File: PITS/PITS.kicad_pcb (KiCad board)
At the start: 4 copper layers, 65 x 56 mm, 75 parts, among them P1 CONN_02X20, P10 I2C, P11 I2C, P12 I2C, P13 I2C, P14 BATT, P2 BNC, P3 BNC, P4 BNC, P5 BNC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

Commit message: first finished layout
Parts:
- removed P10, P11, P12, P13: I2C, Socket_Strips:Socket_Strip_Straight_1x04
- removed P7, P8, P9: 1-WIRE, Socket_Strips:Socket_Strip_Straight_1x03
- removed Q3: BC557, TO_SOT_Packages_SMD:SOT-23
- removed R24, R25, R8: 4k7, Resistors_SMD:R_0805_HandSoldering
- added U8: BME280, RF_Modules:BME280, F.Cu at (95.9, 75.0)
- C1, C2, C4: footprint Capacitors_SMD:C_0805_HandSoldering -> Capacitors_SMD:C_0603_HandSoldering; moved to B.Cu
- C10, C11, C12, C13, C15, C16, C17, C3, C9, L2, Q1, R10, R11, R16, R17, R18, R7, R9, U5: moved to B.Cu
- C14: footprint Capacitors_SMD:C_0805_HandSoldering -> Capacitors_SMD:C_0603_HandSoldering
- D1, D2, D3, D4, D5, D6: footprint LEDs:LED_0805 -> LEDs:LED_0603
- P14: footprint Connectors_Terminal_Blocks:TerminalBlock_Pheonix_MKDS1.5-2pol -> Connectors:SMD_2
- Q2: value BC557 -> Q_PNP_dual; footprint TO_SOT_Packages_SMD:SOT-23 -> TO_SOT_Packages_SMD:SOT-23-6_Handsoldering; moved to B.Cu
- R1, R14, R15, R2, R20, R21, R22, R23, R26, R3, R4, R5: footprint Resistors_SMD:R_0805_HandSoldering -> Resistors_SMD:R_0603_HandSoldering
- R12, R13, R19, R6: footprint Resistors_SMD:R_0805_HandSoldering -> Resistors_SMD:R_0603_HandSoldering; moved to B.Cu
- moved R9 102.3 mm to (84.5, 71.6), turned to 90 degrees
- moved R11 98.7 mm to (94.0, 72.7)
- moved C17 98.0 mm to (87.6, 61.5), turned to 90 degrees
- moved C9 93.9 mm to (99.7, 65.1), turned to 270 degrees
- moved R17 92.5 mm to (96.3, 56.5), turned to 0 degrees
- moved C10 92.1 mm to (85.1, 63.4), turned to 90 degrees
- moved R16 90.7 mm to (96.3, 58.4)
- moved L2 90.0 mm to (104.8, 68.6), turned to 90 degrees
- moved C15 89.6 mm to (93.3, 75.9)
- moved U5 89.4 mm to (93.1, 66.4)
- moved R18 88.4 mm to (96.3, 60.3), turned to 0 degrees
- moved C16 88.4 mm to (93.3, 59.4), turned to 270 degrees
- moved Q1 87.0 mm to (81.9, 61.4), turned to 180 degrees
- moved C3 86.7 mm to (99.7, 68.9), turned to 270 degrees
- moved C13 84.1 mm to (87.6, 68.9), turned to 90 degrees
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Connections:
- C13 pad 1: Net-(C12-Pad2) -> Net-(C13-Pad1)
- C13 pad 2: Net-(C13-Pad2) -> Net-(C12-Pad1)
- Q2 pad 3: +5V_PSU -> Net-(Q2-Pad1)
- R10 pad 1: Net-(C13-Pad2) -> Net-(C12-Pad2)
- R10 pad 2: Net-(C12-Pad1) -> Net-(C13-Pad1)
- R15 pad 1: /GPIO19(MISO1) -> /GPIO20(MOSI1)
- R16 pad 1: Net-(C13-Pad2) -> Net-(C12-Pad1)
- R17 pad 2: Net-(C13-Pad2) -> Net-(C12-Pad1)
- R18 pad 2: Net-(C13-Pad2) -> Net-(C12-Pad1)
- U1 pad 4: /GPIO23 -> /GPIO25
- U2 pad 16: /GPIO27 -> /GPIO16(CE2)
- U2 pad 17: /GPIO22 -> /GPIO19(MISO1)
- U2 pad 4: /GPIO20(MOSI1) -> /GPIO12
- U4 pad 14: /GPIO16(CE2) -> /GPIO22
- U4 pad 7: /GPIO12 -> /GPIO27
- U5 pad 2: Net-(C12-Pad2) -> Net-(C13-Pad1)
- U5 pad 3: Net-(C13-Pad2) -> Net-(C12-Pad1)
- U6 pad 14: /GPIO25 -> /GPIO24
- U6 pad 7: /GPIO24 -> /GPIO23
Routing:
- net GND: track 205.8 -> 483.5 mm, vias 0 -> 3
- net +3V3: track 2.61 -> 91.6 mm, vias 0 -> 4
- net /GPIO27: track 0.00 -> 54.3 mm, vias 0 -> 1
- net +BATT: track 16.5 -> 68.5 mm, vias 0 -> 4
- net /GPIO2(SDA1): track 0.00 -> 50.8 mm, vias 0 -> 4
- net /GPIO16(CE2): track 83.9 -> 33.4 mm, vias 0 -> 1
- net /GPIO3(SCL1): track 0.00 -> 42.1 mm, vias 0 -> 4
- net +5V: track 0.00 -> 38.6 mm
- net /GPIO22: track 0.00 -> 37.5 mm, vias 0 -> 1
- net /GPIO23: track 9.16 -> 37.4 mm, vias 0 -> 1
- net /GPIO12: track 58.4 -> 31.2 mm, vias 0 -> 1
- net /GPIO25: track 36.0 -> 9.14 mm
- net Net-(C12-Pad1): track 1.98 -> 24.0 mm, vias 0 -> 2
- net /GPIO24: track 35.3 -> 17.5 mm, vias 0 -> 1
- net Iout: track 0.00 -> 17.7 mm, vias 0 -> 2
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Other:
- copper layers 4 -> 2

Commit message: old layout - commit for backup
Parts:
- D3: value INTERNET_Green -> Inet_Green
- moved D1 10.5 mm to (99.1, 78.7)
- moved D5 10.5 mm to (109.2, 78.7)
- moved R14 10.2 mm to (99.1, 75.2)
- moved R22 10.2 mm to (109.2, 75.2)
- moved R5 7.29 mm to (81.3, 83.0), turned to 90 degrees
- moved R3 5.72 mm to (81.3, 78.9), turned to 90 degrees
- moved D2 5.68 mm to (101.6, 78.7)
- moved R15 5.18 mm to (101.6, 75.2)
- moved D3 3.59 mm to (106.7, 78.7)
- moved D4 3.59 mm to (104.1, 78.7)
- moved R20 2.74 mm to (106.7, 75.2)
- moved R21 2.74 mm to (104.1, 75.2)
- moved D6 2.54 mm to (111.8, 78.7)
- moved R23 1.03 mm to (111.8, 75.2)
- moved C14 1.00 mm to (96.5, 76.5)
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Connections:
- R14 pad 1: /GPIO26 -> /GPIO5
- R15 pad 1: /GPIO20(MOSI1) -> /GPIO6
- R20 pad 1: /GPIO13 -> /GPIO20(MOSI1)
- R21 pad 1: /GPIO6 -> /GPIO13
- R22 pad 1: /GPIO5 -> /GPIO26
- U2 pad 16: /GPIO16(CE2) -> /GPIO19(MISO1)
- U2 pad 17: /GPIO19(MISO1) -> /GPIO16(CE2)
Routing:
- net GND: track 483.5 -> 305.5 mm, vias 3 -> 1
- net +BATT: track 68.5 -> 6.12 mm, vias 4 -> 0
- net +3V3: track 91.6 -> 109.5 mm, vias 4 -> 5
- net /GPIO2(SDA1): track 50.8 -> 65.3 mm, vias 4 -> 3
- net Net-(R1-Pad1): track 7.76 -> 0.00 mm
- net /GPIO18: track 8.45 -> 1.27 mm, vias 1 -> 0
- net /GPIO15(RXD0): track 64.5 -> 58.7 mm, vias 4 -> 3
- net /GPIO9(MISO0): track 58.9 -> 62.2 mm
- net /GPIO11(SCLK0): track 65.8 -> 68.4 mm
- net /GPIO3(SCL1): track 42.1 -> 44.7 mm, vias 4 -> 3
- net Net-(L1-Pad2): track 2.54 -> 0.00 mm
- net /GPIO7(CE1): track 64.8 -> 67.1 mm
- net /GPIO14(TXD0): track 57.1 -> 59.5 mm, vias 5 -> 3
- net /GPIO25: track 9.14 -> 6.92 mm
- net /GPIO17: track 46.1 -> 43.9 mm
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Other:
- net class Default: trace_width 0.3556 -> 0.254; via_dia 0.5 -> 0.6096; via_drill 0.3 -> 0.3048
- net class POWER: clearance 0.2032 -> 0.03556; trace_width 0.9144 -> 0.6096; via_dia 0.7 -> 1.2192; via_drill 0.5 -> 0.6096
- rule via_min_drill: 0.3 -> 0.3048
- rule via_min_size: 0.4 -> 0.6096

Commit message: working on layout
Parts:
- added P10, P11, P12, P13: I2C, Socket_Strips:Socket_Strip_Straight_1x04, F.Cu at (87.5, 115.1)
- added P7, P8, P9: 1-WIRE, Socket_Strips:Socket_Strip_Straight_1x03, F.Cu at (87.5, 115.1)
- added R24, R25, R8: 4k7, Resistors_SMD:R_0603_HandSoldering, F.Cu at (87.5, 115.1)
- P2, P3, P4, P5, P6: footprint Connectors:SMA_Edge -> Connectors:SMA_Edge_small
- moved C10 145.2 mm to (224.1, 21.4)
- moved C11 145.2 mm to (236.2, 29.1)
- moved C12 145.2 mm to (225.0, 26.9)
- moved C13 145.2 mm to (226.6, 26.9)
- moved C16 145.2 mm to (232.3, 17.4)
- moved C17 145.2 mm to (226.6, 19.5)
- moved C3 145.2 mm to (238.7, 26.9)
- moved C9 145.2 mm to (238.7, 23.1)
- moved L2 145.2 mm to (243.8, 26.6)
- moved Q1 145.2 mm to (220.9, 19.4)
- moved Q2 145.2 mm to (220.9, 24.8)
- moved R10 145.2 mm to (226.5, 30.4)
- moved R11 145.2 mm to (233.0, 30.7)
- moved R16 145.2 mm to (235.3, 16.4)
- moved R18 145.2 mm to (235.3, 18.3)
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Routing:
- net GND: track 305.5 -> 0.00 mm, vias 1 -> 0
- net +3V3: track 109.5 -> 0.00 mm, vias 5 -> 0
- net /GPIO11(SCLK0): track 68.4 -> 0.00 mm, vias 2 -> 0
- net /GPIO7(CE1): track 67.1 -> 0.00 mm, vias 1 -> 0
- net /GPIO2(SDA1): track 65.3 -> 0.00 mm, vias 3 -> 0
- net /GPIO9(MISO0): track 62.2 -> 0.00 mm, vias 2 -> 0
- net /GPIO14(TXD0): track 59.5 -> 0.00 mm, vias 3 -> 0
- net /GPIO10(MOSI0): track 59.3 -> 0.00 mm, vias 2 -> 0
- net /GPIO15(RXD0): track 58.7 -> 0.00 mm, vias 3 -> 0
- net /GPIO27: track 54.2 -> 0.00 mm, vias 1 -> 0
- net /GPIO3(SCL1): track 44.7 -> 0.00 mm, vias 3 -> 0
- net /GPIO17: track 43.9 -> 0.00 mm, vias 1 -> 0
- net /GPIO8(CE0): track 41.7 -> 0.00 mm, vias 1 -> 0
- net +5V: track 37.6 -> 0.00 mm
- net /GPIO22: track 37.3 -> 0.00 mm, vias 1 -> 0
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
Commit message: layout - work in progress
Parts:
- moved U1 146.5 mm to (62.1, 65.8), turned to 270 degrees
- moved U6 87.9 mm to (72.9, 89.1)
- moved P4 64.6 mm to (117.6, 93.1), turned to 180 degrees
- moved P3 62.8 mm to (57.4, 68.4), turned to 0 degrees
- moved U4 52.6 mm to (72.9, 68.1)
- moved P2 36.8 mm to (92.6, 102.0), turned to 90 degrees
- moved U3 36.7 mm to (113.4, 93.6), turned to 90 degrees
- moved P5 31.4 mm to (57.4, 60.1)
- moved P6 17.6 mm to (57.4, 81.1)
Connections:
- net Net-(D1-Pad2) renamed /D1
- net Net-(D2-Pad2) renamed /D2
- net Net-(D3-Pad2) renamed /D3
- net Net-(D4-Pad2) renamed /D4
- net Net-(D5-Pad2) renamed /D5
- net Net-(D6-Pad2) renamed /D6
- net Net-(R2-Pad1) renamed /MTX2-TXD
- net Net-(R26-Pad2) renamed /HX1-TXD
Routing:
- net GND: track 0.00 -> 57.9 mm
- net Net-(P6-Pad1): track 0.00 -> 8.59 mm
- net Net-(P5-Pad1): track 0.00 -> 8.59 mm
- net Net-(P3-Pad1): track 0.00 -> 4.78 mm
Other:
- net class Analog added: clearance 0.2032, trace_width 0.254, via_dia 0.6096, via_drill 0.3048
- net class Digital added: clearance 0.254, trace_width 0.3556, via_dia 0.6096, via_drill 0.3048
- net class HF added: clearance 0.2032, trace_width 1.524, via_dia 0.6096, via_drill 0.3048
- net class NC added: clearance 0.2032, trace_width 0.254, via_dia 0.6096, via_drill 0.3048
- net class POWER: trace_width 0.6096 -> 1.524

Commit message: layout - work in progress
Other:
- net class Digital: clearance 0.254 -> 0.2032; trace_width 0.3556 -> 0.254
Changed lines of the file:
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@@
   (general
     (links 214)
-    (no_connects 193)
-    (area 54.924999 48.924999 120.075001 105.075001)
+    (no_connects 184)
+    (area 49.841238 13.491 251.289 118.294001)
     (thickness 1.6)
     (drawings 14)
@@
   )
   (net_class Digital ""
-    (clearance 0.254)
-    (trace_width 0.3556)
+    (clearance 0.2032)
+    (trace_width 0.254)
     (via_dia 0.6096)
     (via_drill 0.3048)

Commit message: layout - work in progress
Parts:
- removed C10: 10µ, Capacitors_SMD:C_1206_HandSoldering
- removed C11: 1µ, Capacitors_SMD:C_0603_HandSoldering
- removed C12: 680p, Capacitors_SMD:C_0603_HandSoldering
- removed C13, C15: 22p, Capacitors_SMD:C_0603_HandSoldering
- removed C16: 47p, Capacitors_SMD:C_0603_HandSoldering
- removed C17: 47µ, Capacitors_SMD:C_1206_HandSoldering
- removed C3, C9: 100n, Capacitors_SMD:C_0603_HandSoldering
- removed L2: 4.7µH, Inductors:Inductor_Wurth_HCI-7040
- removed R10, R11, R18: 10k, Resistors_SMD:R_0603_HandSoldering
- removed R16: 845k, Resistors_SMD:R_0603_HandSoldering
- removed R17: 158k, Resistors_SMD:R_0603_HandSoldering
- removed R7, R9: 1M, Resistors_SMD:R_0603_HandSoldering
- U5: value LTC3112 -> TPS61030; footprint Housings_SSOP:ETSSOP-20-1EP_4.4x6.5mm_Pitch0.65mm -> power:TPS61030
- moved U5 134.8 mm to (104.0, 66.5), turned to 180 degrees
- moved Q1 128.8 mm to (100.1, 63.9), turned to 270 degrees
- moved Q2 121.9 mm to (105.5, 63.9), turned to 180 degrees
- moved R6 116.2 mm to (110.3, 63.2), turned to 0 degrees
- moved R19 115.0 mm to (110.3, 65.1), turned to 0 degrees
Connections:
- U5 pad 1: GND -> +BATT
- U5 pad 2: Net-(C13-Pad1) -> GND
- U5 pad 3: Net-(C12-Pad1) -> +5V_PSU
- U5 pad 4: GND -> (no net)
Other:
- net class POWER: clearance 0.03556 -> 0.2032; trace_width 1.524 -> 1.27

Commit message: layout - work in progress
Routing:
- net +5V: track 0.00 -> 40.8 mm
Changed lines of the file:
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@@
   (general
     (links 174)
-    (no_connects 144)
+    (no_connects 143)
     (area 54.924999 48.924999 120.075001 105.075001)
     (thickness 1.6)
     (drawings 14)
-    (tracks 23)
+    (tracks 29)
     (zones 0)
     (modules 58)
@@
   (gr_arc (start 58 52) (end 55 52) (angle 90) (layer Edge.Cuts) (width 0.15))
   (gr_line (start 58 105) (end 117 105) (angle 90) (layer Edge.Cuts) (width 0.15))
+  (segment (start 63.37 51.23) (end 62.1 51.23) (width 1.27) (layer F.Cu) (net 2))
+  (segment (start 62.1 51.23) (end 61.465 51.865) (width 1.27) (layer F.Cu) (net 2))
+  (segment (start 61.465 51.865) (end 61.465 55.100962) (width 1.27) (layer F.Cu) (net 2))
+  (segment (start 64.005 57.640962) (end 64.005 86.79) (width 1.27) (layer F.Cu) (net 2))
+  (segment (start 61.465 55.100962) (end 64.005 57.640962) (width 1.27) (layer F.Cu) (net 2))
+  (segment (start 64.005 86.79) (end 62.1 88.695) (width 1.27) (layer F.Cu) (net 2))
   (segment (start 57.4748 65.825) (end 62.09 65.825) (width 1.524) (layer B.Cu) (net 5))
   (segment (start 62.09 65.825) (end 62.1 65.835) (width 1.524) (layer B.Cu) (net 5))

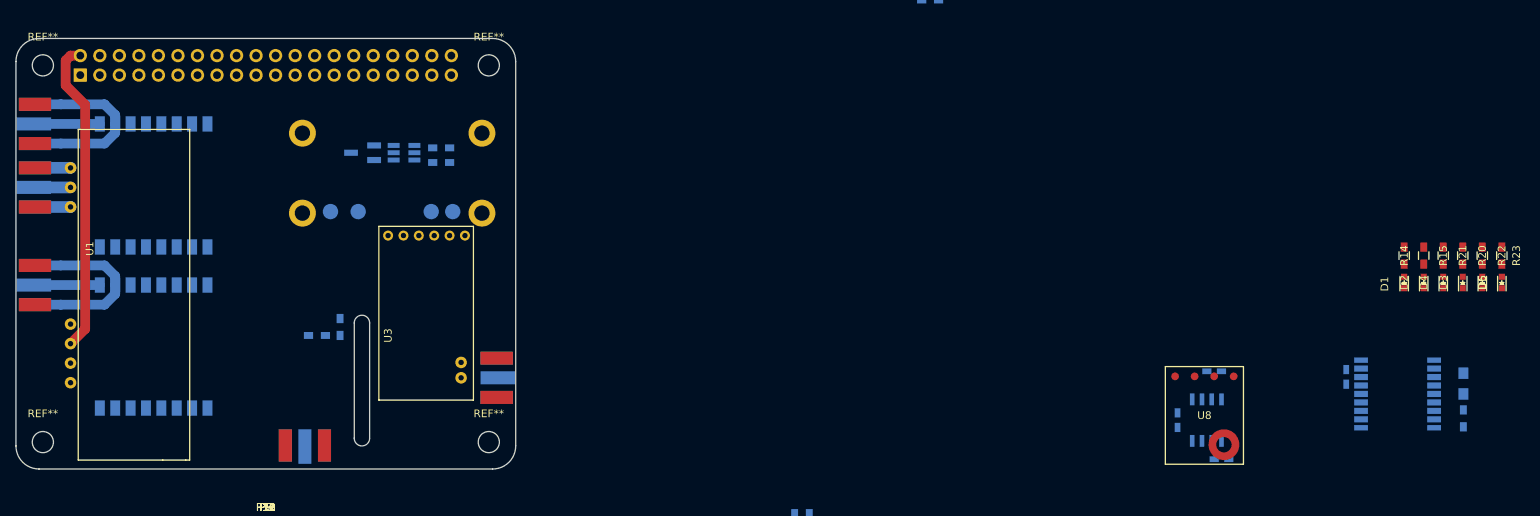
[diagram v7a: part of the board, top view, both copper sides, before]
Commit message: layout for zero - work in progress - backup before pin header change
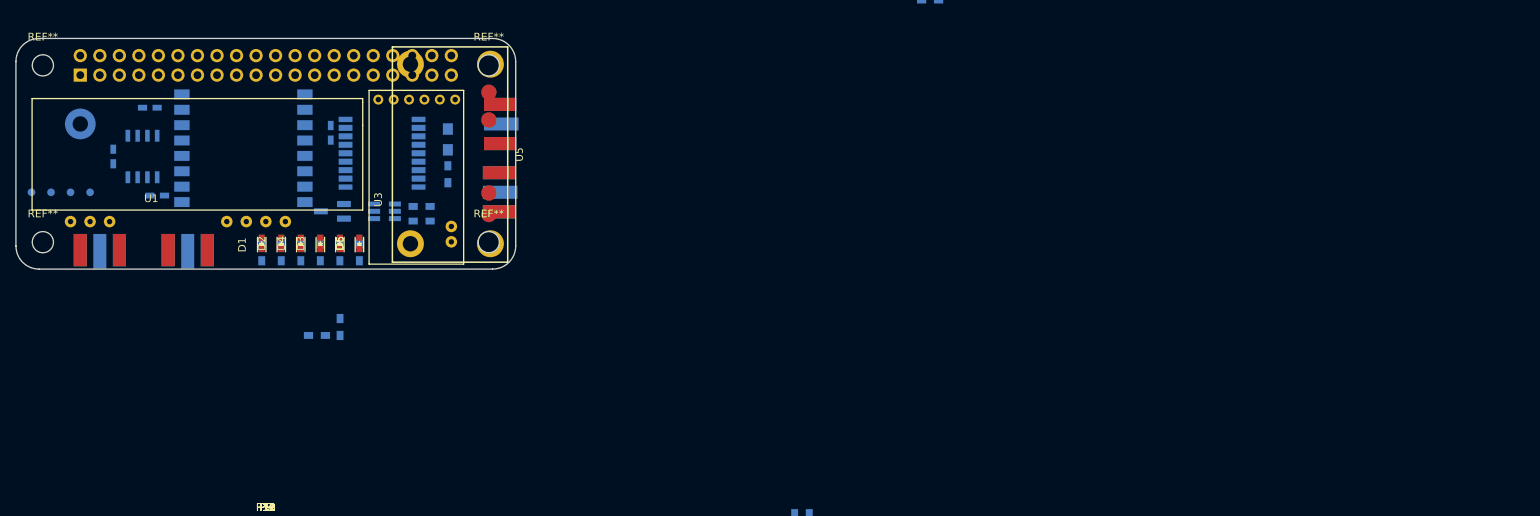
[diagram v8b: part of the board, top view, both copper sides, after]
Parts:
- removed P6: BNC, Connectors:SMA_Edge_small
- removed U6: RFM9*, RF_Modules:RFM9xW
- R14, R15, R20, R21, R22, R23, U8: moved to B.Cu
- U5: moved to F.Cu
- moved U8 150.7 mm to (64.6, 69.0)
- moved D1 148.7 mm to (87.0, 75.7)
- moved D3 148.7 mm to (94.6, 75.7)
- moved D5 148.7 mm to (97.1, 75.7)
- moved D2 148.7 mm to (89.5, 75.7)
- moved D4 148.7 mm to (92.0, 75.7)
- moved D6 148.7 mm to (99.7, 75.7)
- moved R14 148.6 mm to (87.0, 76.8), turned to 90 degrees
- moved R20 148.6 mm to (94.6, 76.8), turned to 90 degrees
- moved R22 148.6 mm to (97.1, 76.8), turned to 90 degrees
- moved R15 148.6 mm to (89.5, 76.8), turned to 90 degrees
- moved R21 148.6 mm to (92.0, 76.8), turned to 90 degrees
- moved R23 148.6 mm to (99.7, 76.8), turned to 90 degrees
- moved C1 142.6 mm to (67.7, 64.4)
- moved C2 142.6 mm to (73.4, 69.4)
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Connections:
- P1 pad 16: /GPIO23 -> (no net)
- P1 pad 18: /GPIO24 -> (no net)
- P1 pad 24: /GPIO8(CE0) -> (no net)
- P1 pad 27: /GPIO0(ID_SD) -> (no net)
- P1 pad 28: /GPIO1(ID_SC) -> (no net)
- U2 pad 13: Net-(U2-Pad13) -> (no net)
- U2 pad 15: Net-(U2-Pad15) -> (no net)
- U2 pad 18: Net-(U2-Pad18) -> (no net)
- U2 pad 5: Net-(U2-Pad5) -> (no net)
- U3 pad 6: Net-(U3-Pad6) -> (no net)
- U3 pad 7: Net-(U3-Pad7) -> (no net)
- U4 pad 11: Net-(U4-Pad11) -> (no net)
- U4 pad 12: Net-(U4-Pad12) -> (no net)
- U4 pad 15: Net-(U4-Pad15) -> (no net)
- U4 pad 16: Net-(U4-Pad16) -> (no net)
- U4 pad 6: Net-(U4-Pad6) -> (no net)
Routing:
- net GND: track 57.9 -> 0.00 mm
- net +5V: track 40.8 -> 0.00 mm
- net Net-(P6-Pad1): track 8.59 -> 0.00 mm
- net Net-(P5-Pad1): track 8.59 -> 0.00 mm
- net Net-(P3-Pad1): track 4.78 -> 0.00 mm
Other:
- board size 65 x 56 mm -> 65 x 30 mm
